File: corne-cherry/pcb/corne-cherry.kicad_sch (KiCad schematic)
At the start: 146 parts, among them J1 MJ-4PP-9, J2 OLED, J3 MJ-4PP-9, J4 OLED, SW1 SW_PUSH, SW10 SW_PUSH, SW11 SW_PUSH, SW12 SW_PUSH, SW13 SW_PUSH, SW14 SW_PUSH, SW15 SW_PUSH, SW16 SW_PUSH, SW17 SW_PUSH, SW18 SW_PUSH, SW19 SW_PUSH, SW2 SW_PUSH, SW20 SW_PUSH, SW21 SW_PUSH, SW22 SW_PUSH, SW23 SW_PUSH, SW24 SW_PUSH, SW25 SW_PUSH, SW26 SW_PUSH, SW27 SW_PUSH, SW28 SW_PUSH, SW29 SW_PUSH, SW3 SW_PUSH, SW30 SW_PUSH, SW31 SW_PUSH, SW32 SW_PUSH, SW33 SW_PUSH, SW34 SW_PUSH, SW35 SW_PUSH, SW36 SW_PUSH, SW37 SW_PUSH, SW38 SW_PUSH, SW39 SW_PUSH, SW4 SW_PUSH, SW40 SW_PUSH, SW41 SW_PUSH, SW42 SW_PUSH, SW5 SW_PUSH, SW6 SW_PUSH, SW7 SW_PUSH, SW8 SW_PUSH, SW9 SW_PUSH, U1 ProMicro, U2 ProMicro

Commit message: Cleanup
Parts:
- removed LED1, LED2, LED28, LED29, LED3, LED30, LED31, LED32, LED33, LED4, LED5, LED6: WS2812B, LED_SMD:LED_WS2812B_PLCC4_5.0x5.0mm_P3.2mm, symbol LED:WS2812B
- removed LED10, LED11, LED12, LED13, LED14, LED15, LED16, LED17, LED18, LED19, LED20, LED21, LED22, LED23, LED24, LED25, LED26, LED27, LED34, LED35, LED36, LED37, LED38, LED39, LED40, LED41, LED42, LED43, LED44, LED45, LED46, LED47, LED48, LED49, LED50, LED51, LED52, LED53, LED54, LED7, LED8, LED9: YS-SK6812MINI-E, kbd:YS-SK6812MINI-E, symbol kbd:YS-SK6812MINI-E
- D1, D10, D11, D12, D13, D14, D15, D16, D17, D18, D19, D2, D20, D21, D22, D23, D24, D25, D26, D27, D28, D29, D3, D30, D31, D32, D33, D34, D35, D36, D37, D38, D39, D4, D40, D41, D42, D5, D6, D7, D8, D9: value D -> 1N4148W
- J1, J3: value MJ-4PP-9 -> PJ320A
- SW1, SW10, SW11, SW12, SW13, SW14, SW15, SW16, SW17, SW18, SW19, SW2, SW20, SW21, SW22, SW23, SW24, SW25, SW26, SW27, SW28, SW29, SW3, SW30, SW31, SW32, SW33, SW34, SW35, SW36, SW37, SW38, SW39, SW4, SW40, SW41, SW42, SW5, SW6, SW7, SW8, SW9: value SW_PUSH -> C5333465
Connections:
- net LED: no longer names the net of U1.1 (TX0/D3)
- net LED_r: no longer names the net of U2.1 (TX0/D3)
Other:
- moved on the sheet: D1, D10, D11, D12, D13, D14, D15, D16, D17, D18, D19, D2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

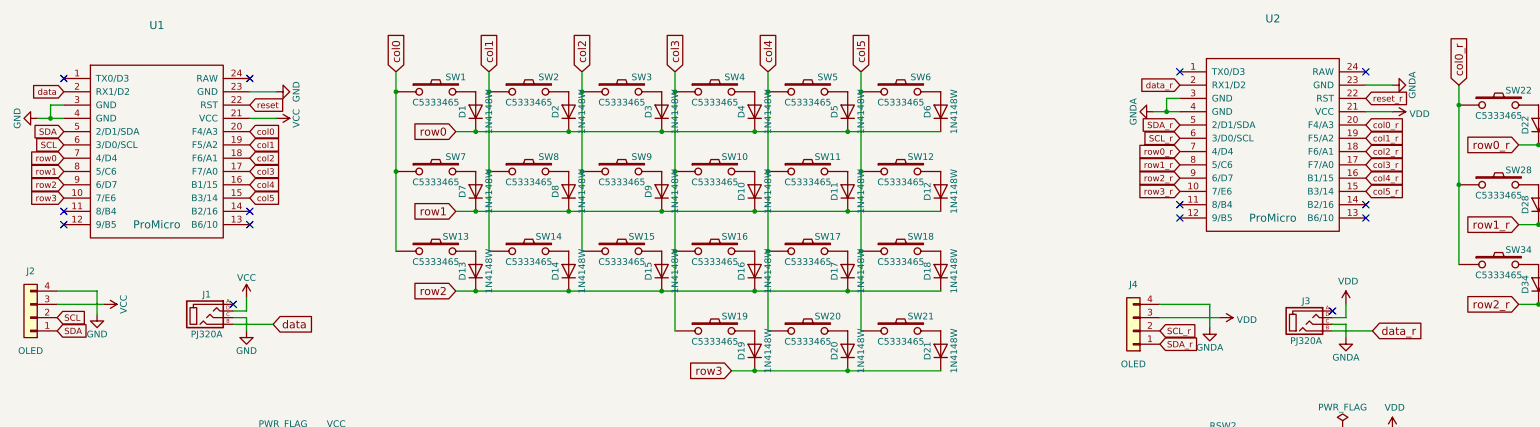
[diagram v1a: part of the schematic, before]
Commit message: Add connection on the missing TRRS
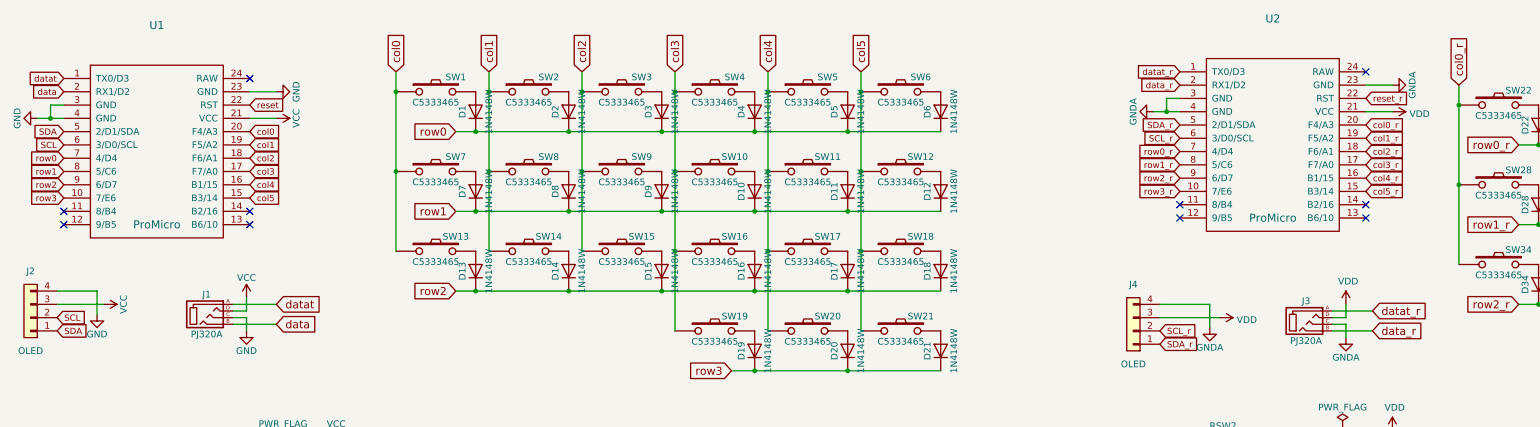
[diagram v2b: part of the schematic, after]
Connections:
- net datat: now reaches U1.1 (TX0/D3)
- net datat: now also J1.A
- net datat_r: now reaches U2.1 (TX0/D3)
- net datat_r: now also J3.A
- no-connect marks 14 -> 10
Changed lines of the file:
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@@
   (no_connect (at 63.5 55.88))
   (no_connect (at 241.3 57.15))
-  (no_connect (at 60.325 73.66))
   (no_connect (at 241.3 54.61))
   (no_connect (at 276.86 54.61))
-  (no_connect (at 241.3 29.21))
   (no_connect (at 27.94 58.42))
-  (no_connect (at 27.94 30.48))
-  (no_connect (at 270.51 74.93))
   (no_connect (at 276.86 29.21))
   (no_connect (at 27.94 55.88))
@@
     (stroke (width 0) (type default))
   )
+  (wire (pts (xy 60.325 73.66) (xy 68.58 73.66))
+    (stroke (width 0) (type default))
+  )
   (wire (pts (xy 345.44 43.18) (xy 363.22 43.18))
     (stroke (width 0) (type default))
@@
     (stroke (width 0) (type default))
   )
-  (wire (pts (xy 60.325 77.47) (xy 67.945 77.47))
+  (wire (pts (xy 60.325 77.47) (xy 68.58 77.47))
     (stroke (width 0) (type default))
   )
@@
     (stroke (width 0) (type default))
   )
+  (wire (pts (xy 270.51 74.93) (xy 278.13 74.93))
+    (stroke (width 0) (type default))
+  )
   (wire (pts (xy 309.88 43.18) (xy 327.66 43.18))
     (stroke (width 0) (type default))
@@
     )
   )
+  (global_label "datat_r" (shape input) (at 278.13 74.93 0) (fields_autoplaced)
+    (effects (font (size 1.524 1.524)) (justify left))
+    (property "Intersheetrefs" "${INTERSHEET_REFS}" (at 288.9098 74.93 0)
+      (effects (font (size 1.27 1.27)) (justify left) hide)
+    )
+  )
   (global_label "col0_r" (shape input) (at 294.64 31.75 90) (fields_autoplaced)
     (effects (font (size 1.524 1.524)) (justify left))
@@
     )
   )
+  (global_label "datat" (shape input) (at 27.94 30.48 180) (fields_autoplaced)
+    (effects (font (size 1.1938 1.1938)) (justify right))
+    (property "Intersheetrefs" "${INTERSHEET_REFS}" (at 21.1444 30.48 0)
+      (effects (font (size 1.27 1.27)) (justify right) hide)
+    )
+  )
   (global_label "col1_r" (shape input) (at 276.86 41.91 0) (fields_autoplaced)
     (effects (font (size 1.1938 1.1938)) (justify left))
@@
     )
   )
+  (global_label "datat" (shape input) (at 68.58 73.66 0) (fields_autoplaced)
+    (effects (font (size 1.524 1.524)) (justify left))
+    (property "Intersheetrefs" "${INTERSHEET_REFS}" (at 77.2553 73.66 0)
+      (effects (font (size 1.27 1.27)) (justify left) hide)
+    )
+  )
   (global_label "col4_r" (shape input) (at 365.76 31.75 90) (fields_autoplaced)
     (effects (font (size 1.524 1.524)) (justify left))
@@
     )
   )
+  (global_label "datat_r" (shape input) (at 241.3 29.21 180) (fields_autoplaced)
+    (effects (font (size 1.1938 1.1938)) (justify right))
+    (property "Intersheetrefs" "${INTERSHEET_REFS}" (at 232.8558 29.21 0)
+      (effects (font (size 1.27 1.27)) (justify right) hide)
+    )
+  )
   (global_label "col2" (shape input) (at 63.5 45.72 0) (fields_autoplaced)
     (effects (font (size 1.1938 1.1938)) (justify left))
@@
     )
   )
-  (global_label "data" (shape input) (at 67.945 77.47 0) (fields_autoplaced)
-    (effects (font (size 1.524 1.524)) (justify left))
-    (property "Intersheetrefs" "${INTERSHEET_REFS}" (at 75.7494 77.47 0)
-      (effects (font (size 1.27 1.27)) (justify left) hide)
-    )
+  (global_label "data" (shape input) (at 68.58 77.47 0) (fields_autoplaced)
+    (effects (font (size 1.524 1.524)) (justify left))
+    (property "Intersheetrefs" "${INTERSHEET_REFS}" (at 76.3844 77.47 0)
+      (effects (font (size 1.27 1.27)) (justify left) hide)
+    )
